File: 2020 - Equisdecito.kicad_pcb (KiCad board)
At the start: 2 copper layers, 60 x 40 mm, 36 parts, among them J1 VL53L0x_IZQ, J10 IMU, J11 Batería (-), J12 sharp2, J13 sharp2, J14 Arduino_Nano_Header, J15 sharp2, J16 MOTOR 1, J17 sharp2, J18 MOTOR 2, J19 AUX6, J2 VL53L0x_DER, J3 HC-05, J4 Pantalla Oled, J5 Batería (+), J6 sharp1, J7 tatami 1, J8 tatami 2, J9 Aux1, Q1 2N7002, SW1 Pulsador, U1 LM1117-SOT

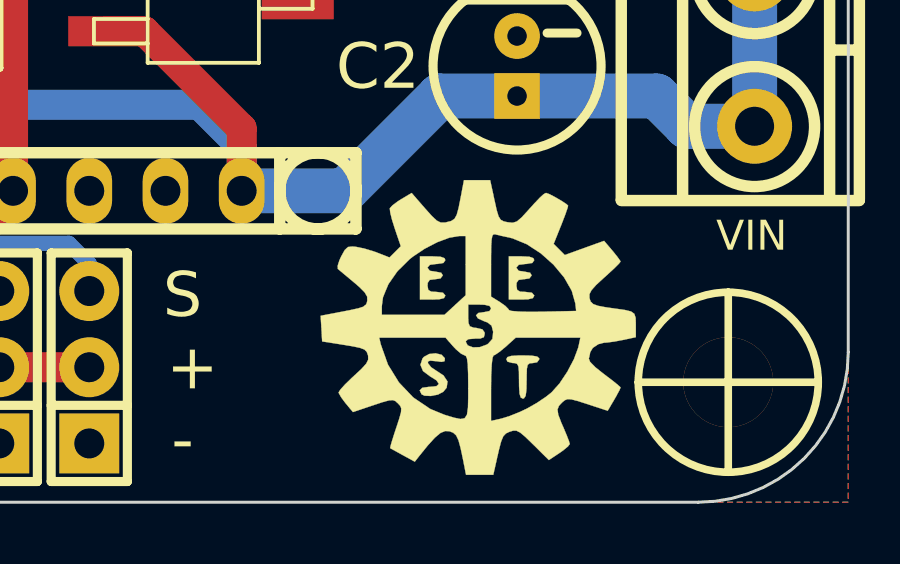
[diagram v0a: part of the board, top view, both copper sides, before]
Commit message: MODIFICACIONES
se quito un logo en la capa bottom,se agrego descripción en el sch, y por ultimo se agrego revisión
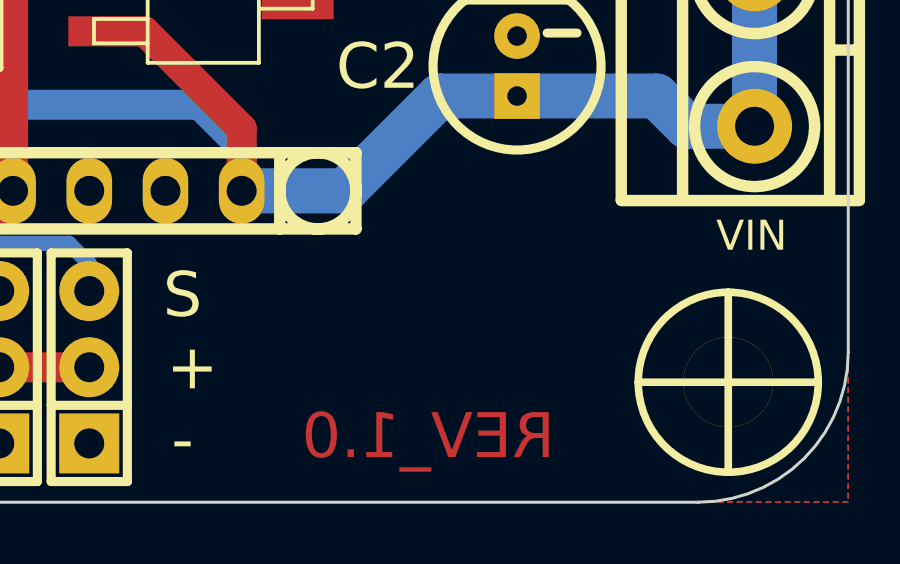
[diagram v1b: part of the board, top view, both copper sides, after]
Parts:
- removed LG2: Mounting_Hole, EESTN5:LOGO_EESTN5
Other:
- board text added: "REV_1.0"
- board text removed: "ROBOTICA TECNICA 5"
